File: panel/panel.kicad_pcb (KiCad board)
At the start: 2 copper layers, 95 x 95 mm, 6 parts

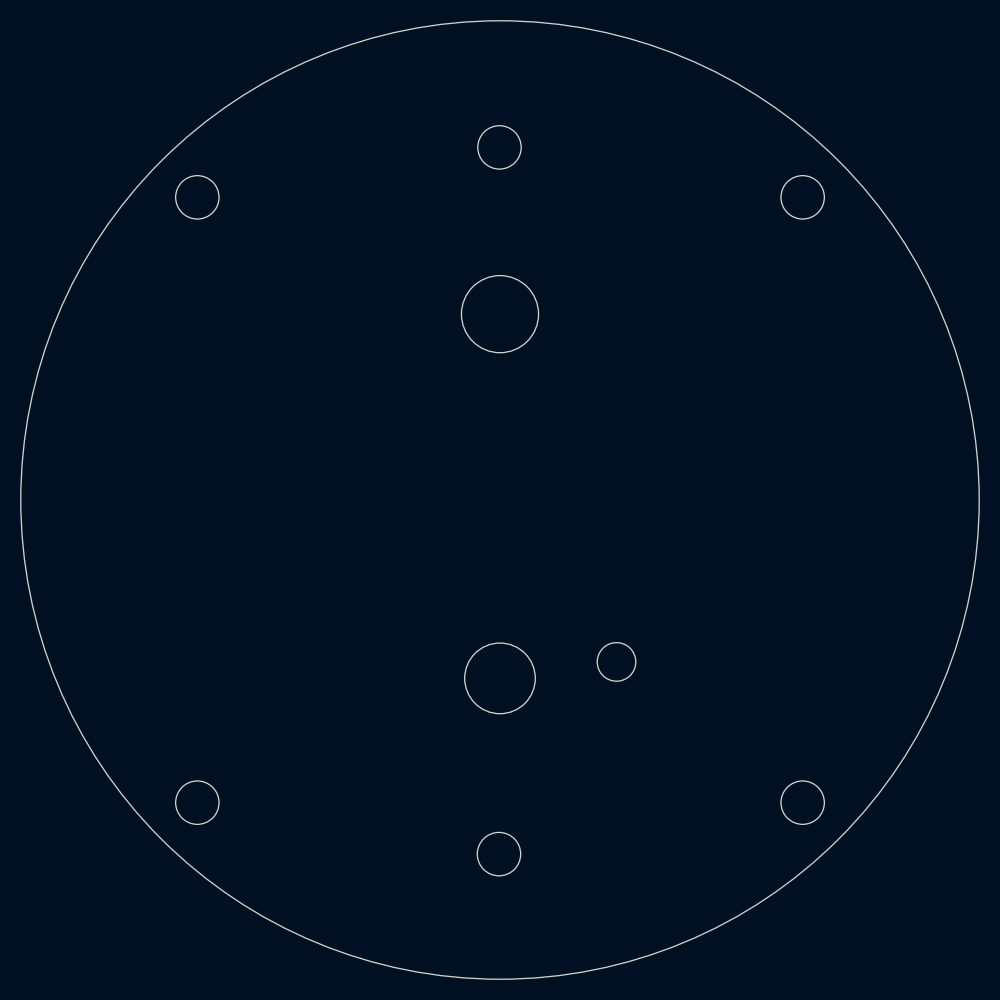
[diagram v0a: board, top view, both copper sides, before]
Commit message: updated circuit and panel to include envelope follower
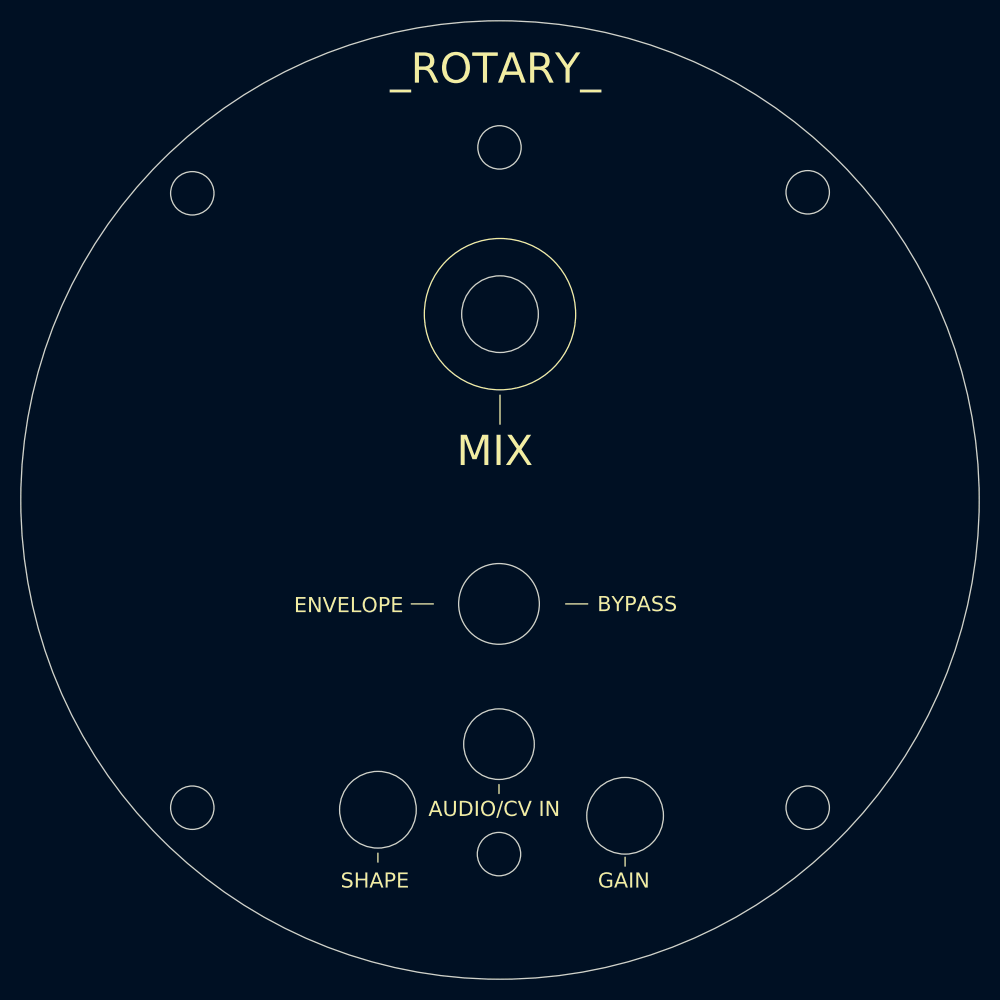
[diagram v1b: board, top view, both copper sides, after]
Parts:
- moved REF** 0.71 mm to (69.5, 130.5)
- moved REF** 0.71 mm to (130.5, 69.5)
- moved REF** 0.71 mm to (130.5, 130.5)
- moved REF** 0.64 mm to (69.5, 69.6)
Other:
- outline, holes or cut-outs redrawn
- board text added: "AUDIO/CV IN"
- board text added: "BYPASS"
- board text added: "ENVELOPE"
- board text added: "GAIN"
- board text added: "MIX"
- board text added: "SHAPE"
- board text added: "_ROTARY_"
- board text added: "_rotary_ panel v1_0_0"
- board text removed: "_rotary_ panel v0_1_2"

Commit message: update pcbs and panels
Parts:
- removed REF** (x6): MountingHole_4.3mm_M4, MountingHole:MountingHole_4.3mm_M4
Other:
- outline, holes or cut-outs redrawn
- board text added: "_rotary_ panel v1_1_1"
- board text removed: "_rotary_ panel v1_0_0"
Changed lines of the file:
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@@
   )
   (net 0 "")
-  (footprint "MountingHole:MountingHole_4.3mm_M4" (layer "F.Cu")
-    (at 99.9 135.1)
-    (descr "Mounting Hole 4.3mm, no annular, M4")
-    (tags "mounting hole 4.3mm no annular m4")
-    (attr exclude_from_pos_files exclude_from_bom)
-    (fp_text reference "REF**" (at 0 -5.3) (layer "F.SilkS") hide
-        (effects (font (size 1 1) (thickness 0.15)))
-    )
-    (fp_text value "MountingHole_4.3mm_M4" (at 0 5.3) (layer "F.Fab") hide
-        (effects (font (size 1 1) (thickness 0.15)))
-    )
-    (fp_circle (center 0 0) (end 4.3 0)
-      (stroke (width 0.15) (type solid)) (fill none) (layer "Cmts.User"))
-    (fp_circle (center 0 0) (end 4.55 0)
-      (stroke (width 0.05) (type solid)) (fill none) (layer "F.CrtYd"))
-    (pad "" np_thru_hole circle (at 0 0) (size 4.3 4.3) (drill 4.3) (layers "*.Cu" "*.Mask"))
-  )
-  (footprint "MountingHole:MountingHole_4.3mm_M4" (layer "F.Cu")
-    (at 69.5 130.5)
-    (descr "Mounting Hole 4.3mm, no annular, M4")
-    (tags "mounting hole 4.3mm no annular m4")
-    (attr exclude_from_pos_files exclude_from_bom)
-    (fp_text reference "REF**" (at 0 -5.3) (layer "F.SilkS") hide
-        (effects (font (size 1 1) (thickness 0.15)))
-    )
-    (fp_text value "MountingHole_4.3mm_M4" (at 0 5.3) (layer "F.Fab") hide
-        (effects (font (size 1 1) (thickness 0.15)))
-    )
-    (fp_text user "${REFERENCE}" (at 0 0) (layer "F.Fab")
-        (effects (font (size 1 1) (thickness 0.15)))
-    )
-    (fp_circle (center 0 0) (end 4.3 0)
-      (stroke (width 0.15) (type solid)) (fill none) (layer "Cmts.User"))
-    (fp_circle (center 0 0) (end 4.55 0)
-      (stroke (width 0.05) (type solid)) (fill none) (layer "F.CrtYd"))
-    (pad "" np_thru_hole circle (at 0 0) (size 4.3 4.3) (drill 4.3) (layers "*.Cu" "*.Mask"))
-  )
-  (footprint "MountingHole:MountingHole_4.3mm_M4" (layer "F.Cu")
-    (at 130.5 69.5)
-    (descr "Mounting Hole 4.3mm, no annular, M4")
-    (tags "mounting hole 4.3mm no annular m4")
-    (attr exclude_from_pos_files exclude_from_bom)
-    (fp_text reference "REF**" (at 0 -5.3) (layer "F.SilkS") hide
-        (effects (font (size 1 1) (thickness 0.15)))
-    )
-    (fp_text value "MountingHole_4.3mm_M4" (at 0 5.3) (layer "F.Fab") hide
-        (effects (font (size 1 1) (thickness 0.15)))
-    )
-    (fp_text user "${REFERENCE}" (at 0 0) (layer "F.Fab")
-        (effects (font (size 1 1) (thickness 0.15)))
-    )
-    (fp_circle (center 0 0) (end 4.3 0)
-      (stroke (width 0.15) (type solid)) (fill none) (layer "Cmts.User"))
-    (fp_circle (center 0 0) (end 4.55 0)
-      (stroke (width 0.05) (type solid)) (fill none) (layer "F.CrtYd"))
-    (pad "" np_thru_hole circle (at 0 0) (size 4.3 4.3) (drill 4.3) (layers "*.Cu" "*.Mask"))
-  )
-  (footprint "MountingHole:MountingHole_4.3mm_M4" (layer "F.Cu")
-    (at 99.95 65.05)
-    (descr "Mounting Hole 4.3mm, no annular, M4")
-    (tags "mounting hole 4.3mm no annular m4")
-    (attr exclude_from_pos_files exclude_from_bom)
-    (fp_text reference "REF**" (at 0 -5.3) (layer "F.SilkS") hide
-        (effects (font (size 1 1) (thickness 0.15)))
-    )
-    (fp_text value "MountingHole_4.3mm_M4" (at 0 5.3) (layer "F.Fab") hide
-        (effects (font (size 1 1) (thickness 0.15)))
-    )
-    (fp_text user "${REFERENCE}" (at 0 0) (layer "F.Fab")
-        (effects (font (size 1 1) (thickness 0.15)))
-    )
-    (fp_circle (center 0 0) (end 4.3 0)
-      (stroke (width 0.15) (type solid)) (fill none) (layer "Cmts.User"))
-    (fp_circle (center 0 0) (end 4.55 0)
-      (stroke (width 0.05) (type solid)) (fill none) (layer "F.CrtYd"))
-    (pad "" np_thru_hole circle (at 0 0) (size 4.3 4.3) (drill 4.3) (layers "*.Cu" "*.Mask"))
-  )
-  (footprint "MountingHole:MountingHole_4.3mm_M4" (layer "F.Cu")
-    (at 69.5 69.6)
-    (descr "Mounting Hole 4.3mm, no annular, M4")
-    (tags "mounting hole 4.3mm no annular m4")
-    (attr exclude_from_pos_files exclude_from_bom)
-    (fp_text reference "REF**" (at 0 -5.3) (layer "F.SilkS") hide
-        (effects (font (size 1 1) (thickness 0.15)))
-    )
-    (fp_text value "MountingHole_4.3mm_M4" (at 0 5.3) (layer "F.Fab") hide
-        (effects (font (size 1 1) (thickness 0.15)))
-    )
-    (fp_text user "${REFERENCE}" (at 0 0) (layer "F.Fab")
-        (effects (font (size 1 1) (thickness 0.15)))
-    )
-    (fp_circle (center 0 0) (end 4.3 0)
-      (stroke (width 0.15) (type solid)) (fill none) (layer "Cmts.User"))
-    (fp_circle (center 0 0) (end 4.55 0)
-      (stroke (width 0.05) (type solid)) (fill none) (layer "F.CrtYd"))
-    (pad "" np_thru_hole circle (at 0 0) (size 4.3 4.3) (drill 4.3) (layers "*.Cu" "*.Mask"))
-  )
-  (footprint "MountingHole:MountingHole_4.3mm_M4" (layer "F.Cu")
-    (at 130.5 130.5)
-    (descr "Mounting Hole 4.3mm, no annular, M4")
-    (tags "mounting hole 4.3mm no annular m4")
-    (attr exclude_from_pos_files exclude_from_bom)
-    (fp_text reference "REF**" (at 0 -5.3) (layer "F.SilkS") hide
-        (effects (font (size 1 1) (thickness 0.15)))
-    )
-    (fp_text value "MountingHole_4.3mm_M4" (at 0 5.3) (layer "F.Fab") hide
-        (effects (font (size 1 1) (thickness 0.15)))
-    )
-    (fp_text user "${REFERENCE}" (at 0 0) (layer "F.Fab")
-        (effects (font (size 1 1) (thickness 0.15)))
-    )
-    (fp_circle (center 0 0) (end 4.3 0)
-      (stroke (width 0.15) (type solid)) (fill none) (layer "Cmts.User"))
-    (fp_circle (center 0 0) (end 4.55 0)
-      (stroke (width 0.05) (type solid)) (fill none) (layer "F.CrtYd"))
-    (pad "" np_thru_hole circle (at 0 0) (size 4.3 4.3) (drill 4.3) (layers "*.Cu" "*.Mask"))
-  )
   (gr_line (start 112.4 135.4) (end 112.4 136.3)
     (stroke (width 0.12) (type default)) (layer "F.SilkS"))
@@
   (gr_line (start 106.5 110.3) (end 108.7 110.3)
     (stroke (width 0.12) (type default)) (layer "F.SilkS"))
-  (gr_circle (center 100 81.579006) (end 107.5 81.579006)
+  (gr_circle (center 100 81.579006) (end 107.4 81.579006)
     (stroke (width 0.05) (type default)) (fill none) (layer "F.SilkS"))
+  (gr_circle (center 99.96 65.02) (end 102.26 65.02)
+    (stroke (width 0.12) (type default)) (fill none) (layer "Edge.Cuts"))
+  (gr_circle (center 99.9 135.09) (end 102.2 135.09)
+    (stroke (width 0.12) (type default)) (fill none) (layer "Edge.Cuts"))
   (gr_circle (center 87.9 130.7) (end 91.7 130.7)
     (stroke (width 0.05) (type default)) (fill none) (layer "Edge.Cuts"))
@@
   (gr_circle (center 100 100) (end 147.5 100)
     (stroke (width 0.12) (type solid)) (fill none) (layer "Edge.Cuts"))
+  (gr_circle (center 130.49 69.58) (end 132.79 69.58)
+    (stroke (width 0.12) (type default)) (fill none) (layer "Edge.Cuts"))
   (gr_circle (center 99.9 124.2) (end 103.4 124.2)
     (stroke (width 0.05) (type default)) (fill none) (layer "Edge.Cuts"))
   (gr_circle (center 100 81.579006) (end 103.8 81.579006)
     (stroke (width 0.05) (type default)) (fill none) (layer "Edge.Cuts"))
+  (gr_circle (center 69.48 130.48) (end 71.78 130.48)
+    (stroke (width 0.12) (type default)) (fill none) (layer "Edge.Cuts"))
+  (gr_circle (center 130.49 130.47) (end 132.79 130.47)
+    (stroke (width 0.12) (type default)) (fill none) (layer "Edge.Cuts"))
   (gr_circle (center 112.4 131.3) (end 116.2 131.3)
     (stroke (width 0.05) (type default)) (fill none) (layer "Edge.Cuts"))
+  (gr_circle (center 69.48 69.58) (end 71.78 69.58)
+    (stroke (width 0.12) (type default)) (fill none) (layer "Edge.Cuts"))
   (gr_text "_^ 12" (at 99.9 138.2) (layer "B.SilkS")
     (effects (font (size 5 5) (thickness 0.5)) (justify mirror))
   )
-  (gr_text "_rotary_ panel\nv1_0_0" (at 99.1 58.4) (layer "B.SilkS")
+  (gr_text "_rotary_ panel\nv1_1_1" (at 99.1 58.4) (layer "B.SilkS")
     (effects (font (size 2 2) (thickness 0.2)) (justify mirror))
   )
